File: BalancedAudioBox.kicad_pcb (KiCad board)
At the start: 2 copper layers, 26 parts, among them IC1 TPS61240IDRVRQ1, IC2 DRV135UA_2K5, J1 Conn_02x10_Odd_Even, U1 LM27762, U2 PCM5102

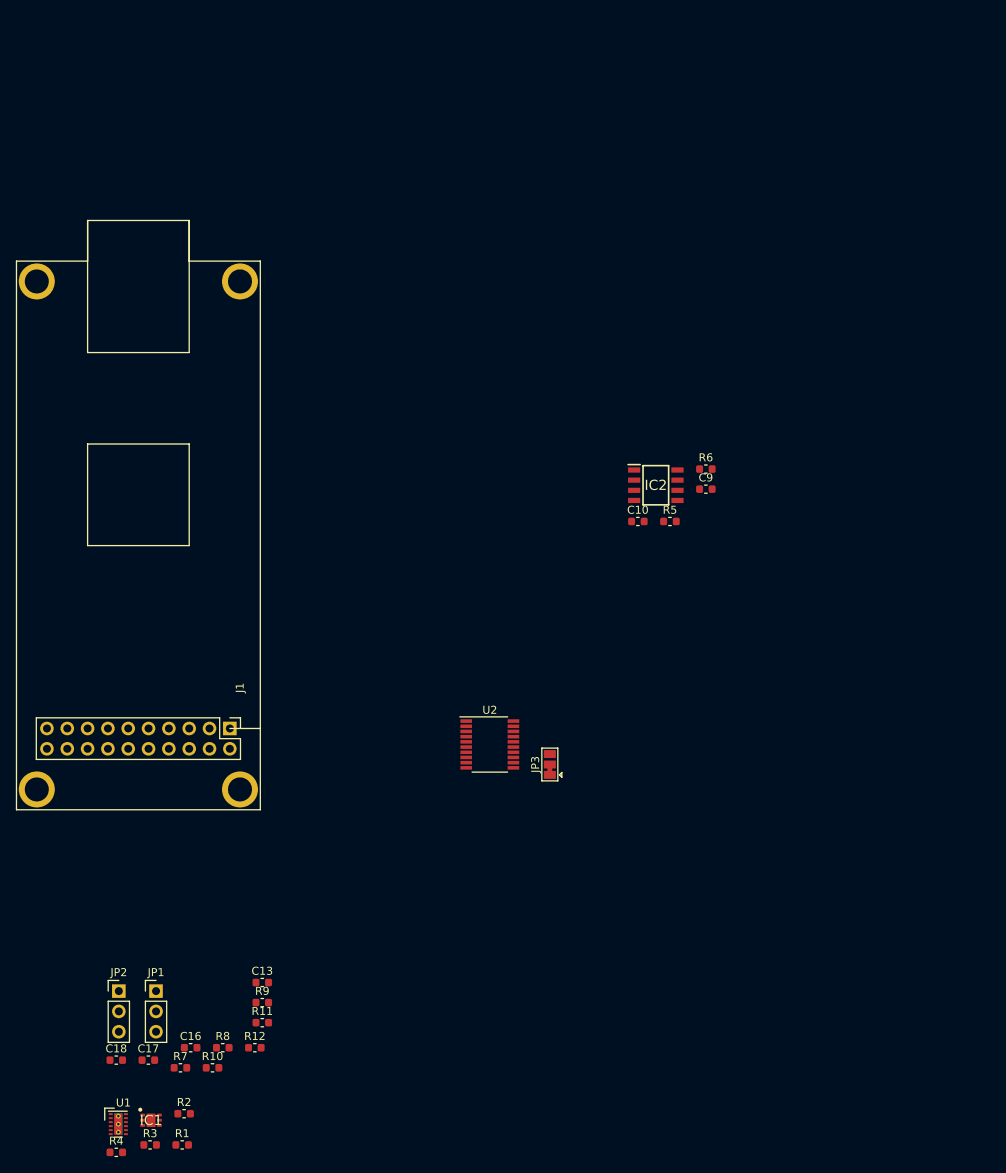
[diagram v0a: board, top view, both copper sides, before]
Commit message: adding PCB libraries
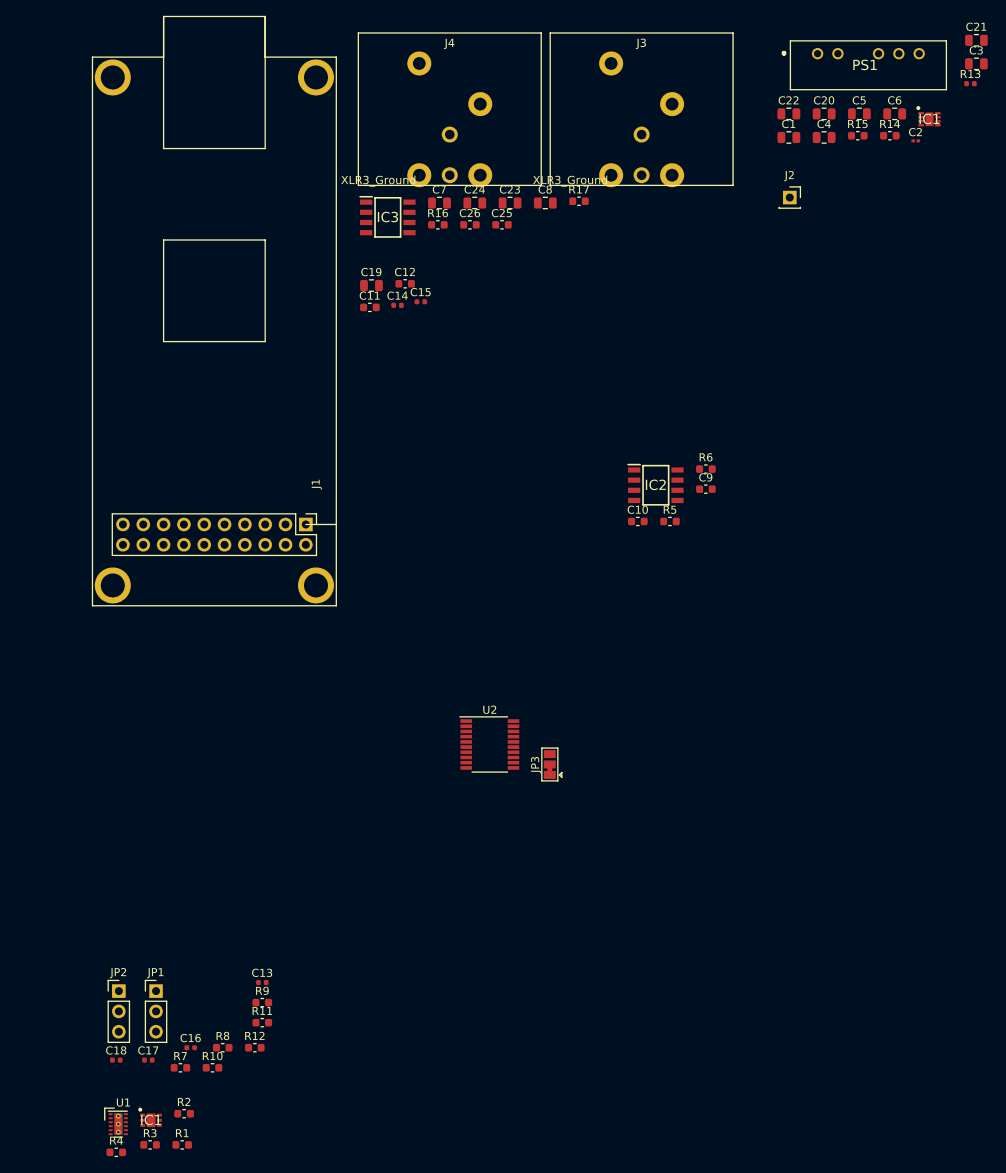
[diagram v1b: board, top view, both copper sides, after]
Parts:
- added C1: 10u/25V, Capacitor_SMD:C_0805_2012Metric, F.Cu at (191.9, 33.6)
- added C11: 2.2u, Capacitor_SMD:C_0603_1608Metric, F.Cu at (139.5, 54.9)
- added C12: 2.2u, Capacitor_SMD:C_0603_1608Metric, F.Cu at (143.9, 51.9)
- added C14: 2.2n, Capacitor_SMD:C_0402_1005Metric, F.Cu at (143.0, 54.6)
- added C15: 2.2n, Capacitor_SMD:C_0402_1005Metric, F.Cu at (145.9, 54.2)
- added C19: 10u/25V, Resistor_SMD:R_0805_2012Metric, F.Cu at (139.7, 52.1)
- added C2: 100p, Capacitor_SMD:C_0201_0603Metric, F.Cu at (207.7, 34.0)
- added C20: 10u/25V, Capacitor_SMD:C_0805_2012Metric, F.Cu at (196.3, 30.7)
- added C21: 4.7u, Capacitor_SMD:C_0805_2012Metric, F.Cu at (215.3, 21.5)
- added C22: 4.7u, Capacitor_SMD:C_0805_2012Metric, F.Cu at (191.9, 30.7)
- added C23: 4.7u, Capacitor_SMD:C_0805_2012Metric, F.Cu at (157.0, 41.8)
- added C24: 4.7u, Capacitor_SMD:C_0805_2012Metric, F.Cu at (152.6, 41.8)
- added C25: 100n, Capacitor_SMD:C_0603_1608Metric, F.Cu at (156.0, 44.5)
- added C26: 100n, Capacitor_SMD:C_0603_1608Metric, F.Cu at (152.0, 44.5)
- added C3: 4.7u, Capacitor_SMD:C_0805_2012Metric, F.Cu at (215.3, 24.4)
- added C4: 10u/25V, Capacitor_SMD:C_0805_2012Metric, F.Cu at (196.3, 33.6)
- added C5: 10u/25V, Capacitor_SMD:C_0805_2012Metric, F.Cu at (200.7, 30.7)
- added C6: 10u/25V, Capacitor_SMD:C_0805_2012Metric, F.Cu at (205.1, 30.7)
- added C7: 4.7u, Capacitor_SMD:C_0805_2012Metric, F.Cu at (148.2, 41.8)
- added C8: 4.7u, Capacitor_SMD:C_0805_2012Metric, F.Cu at (161.4, 41.8)
- added IC1: TPS61252DSGT, SamacSys_PCB_Library:SON50P200X200X80-9N, F.Cu at (209.5, 31.4)
- added IC3: DRV135UA_2K5, SamacSys_PCB_Library:SOIC127P600X175-8N, F.Cu at (141.8, 43.6)
- added J2: Conn_01x02, Connector_PinSocket_2.54mm:PinSocket_1x01_P2.54mm_Vertical, F.Cu at (192.0, 41.1)
- added J3: XLR3_Ground, BalancedAudioBox:XLR-NC3MA, F.Cu at (173.5, 30.1)
- added J4: XLR3_Ground, BalancedAudioBox:XLR-NC3MA, F.Cu at (149.5, 30.1)
- added PS1: DPU01L-15, SamacSys_PCB_Library:DPU01L15, F.Cu at (195.5, 23.2)
- added R13: 47k, Resistor_SMD:R_0402_1005Metric, F.Cu at (214.6, 26.9)
- added R14: 634k, Resistor_SMD:R_0603_1608Metric, F.Cu at (204.5, 33.4)
- added R15: 180k, Resistor_SMD:R_0603_1608Metric, F.Cu at (200.5, 33.4)
- added R16: 300R, Resistor_SMD:R_0603_1608Metric, F.Cu at (148.0, 44.5)
- added R17: 300R, Resistor_SMD:R_0603_1608Metric, F.Cu at (165.6, 41.6)
- C13, C16, C17, C18: footprint Capacitor_SMD:C_0603_1608Metric -> Capacitor_SMD:C_0402_1005Metric
- R1, R2: value R -> 1.58M
- R3, R4: value R -> 499k
- moved J1 27.2 mm to (131.5, 82.0)
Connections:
- C10 pad 1: Net-(C10-Pad1) -> -5V
- C9 pad 1: Net-(C9-Pad1) -> +5V

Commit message: placement complete
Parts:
- removed the IC1 at (112.2, 156.5)
- removed the IC1 at (209.5, 31.4)
- added C27: 10u/25V, Capacitor_SMD:C_0805_2012Metric, F.Cu at (143.0, 96.0)
- added IC1: TPS61252DSGT, BalancedAudioBox:SON50P200X200X80-9N, F.Cu at (148.0, 96.0)
- added J5: Conn_01x03, Connector_PinHeader_2.54mm:PinHeader_1x03_P2.54mm_Vertical, F.Cu at (174.5, 95.0)
- added J6: Conn_01x02, Connector_PinSocket_2.54mm:PinSocket_1x02_P2.54mm_Vertical, F.Cu at (148.0, 107.5)
- added L1: 1.5u, BalancedAudioBox:SRN30151R5Y, F.Cu at (146.6, 91.5)
- C10, C25, C26, C9: footprint Capacitor_SMD:C_0603_1608Metric -> Capacitor_SMD:C_0402_1005Metric
- C11, C12: footprint Capacitor_SMD:C_0603_1608Metric -> Capacitor_SMD:C_0805_2012Metric
- C19: footprint Resistor_SMD:R_0805_2012Metric -> Capacitor_SMD:C_0805_2012Metric
- C2: footprint Capacitor_SMD:C_0201_0603Metric -> Capacitor_SMD:C_0603_1608Metric
- IC2, IC3: footprint SamacSys_PCB_Library:SOIC127P600X175-8N -> Package_SO:SOIC-8_3.9x4.9mm_P1.27mm
- J2: value Conn_01x02 -> Conn_01x03; footprint Connector_PinSocket_2.54mm:PinSocket_1x01_P2.54mm_Vertical -> Connector_PinHeader_2.54mm:PinHeader_1x03_P2.54mm_Vertical
- PS1: footprint SamacSys_PCB_Library:DPU01L15 -> BalancedAudioBox:DPU01L15
- R10, R11, R12, R7, R8, R9: footprint Resistor_SMD:R_0603_1608Metric -> Resistor_SMD:R_0402_1005Metric
- moved PS1 119.1 mm to (145.0, 131.0)
- moved C21 115.0 mm to (145.0, 112.5), turned to 180 degrees
- moved C3 113.1 mm to (147.0, 114.5)
- moved C20 102.7 mm to (147.5, 121.0), turned to 270 degrees
- moved C6 98.7 mm to (147.0, 110.5), turned to 180 degrees
- moved C22 98.7 mm to (150.0, 120.0), turned to 90 degrees
- moved R13 93.3 mm to (152.5, 96.5), turned to 270 degrees
- moved C5 91.2 mm to (146.5, 104.0), turned to 180 degrees
- moved C19 86.6 mm to (181.5, 128.0)
- moved C2 86.4 mm to (152.5, 100.5), turned to 90 degrees
- moved R14 86.1 mm to (150.5, 100.5), turned to 90 degrees
- moved C4 84.2 mm to (146.5, 101.5), turned to 180 degrees
- moved R15 80.9 mm to (150.5, 97.0), turned to 90 degrees
- moved C1 78.0 mm to (145.0, 96.0), turned to 270 degrees
- moved C18 77.0 mm to (181.0, 125.0)
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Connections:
- net Net-(C2-Pad1) renamed /PowerSupply/VOUT-5.4V
- net Net-(C2-Pad2) renamed /PowerSupply/FB
- net Net-(C20-Pad1) renamed /PowerSupply/CP
- net Net-(R1-Pad2) renamed /PowerSupply/FB+
- net Net-(R2-Pad2) renamed /PowerSupply/FB-
- J2 pad 1: /PowerSupply/VIN -> +3V3
- PS1 pad 1: Net-(PS1-Pad1) -> /PowerSupply/VIN
- PS1 pad 2: Net-(PS1-Pad2) -> GND
- PS1 pad 4: Net-(PS1-Pad4) -> -5V
- PS1 pad 5: Net-(PS1-Pad5) -> GND
- PS1 pad 6: Net-(PS1-Pad6) -> +5V
- R13 pad 2: Net-(IC1-Pad4) -> /PowerSupply/ILIM
- R7 pad 1: Net-(R7-Pad1) -> +3V3
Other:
- board outline added: 90 x 80 mm

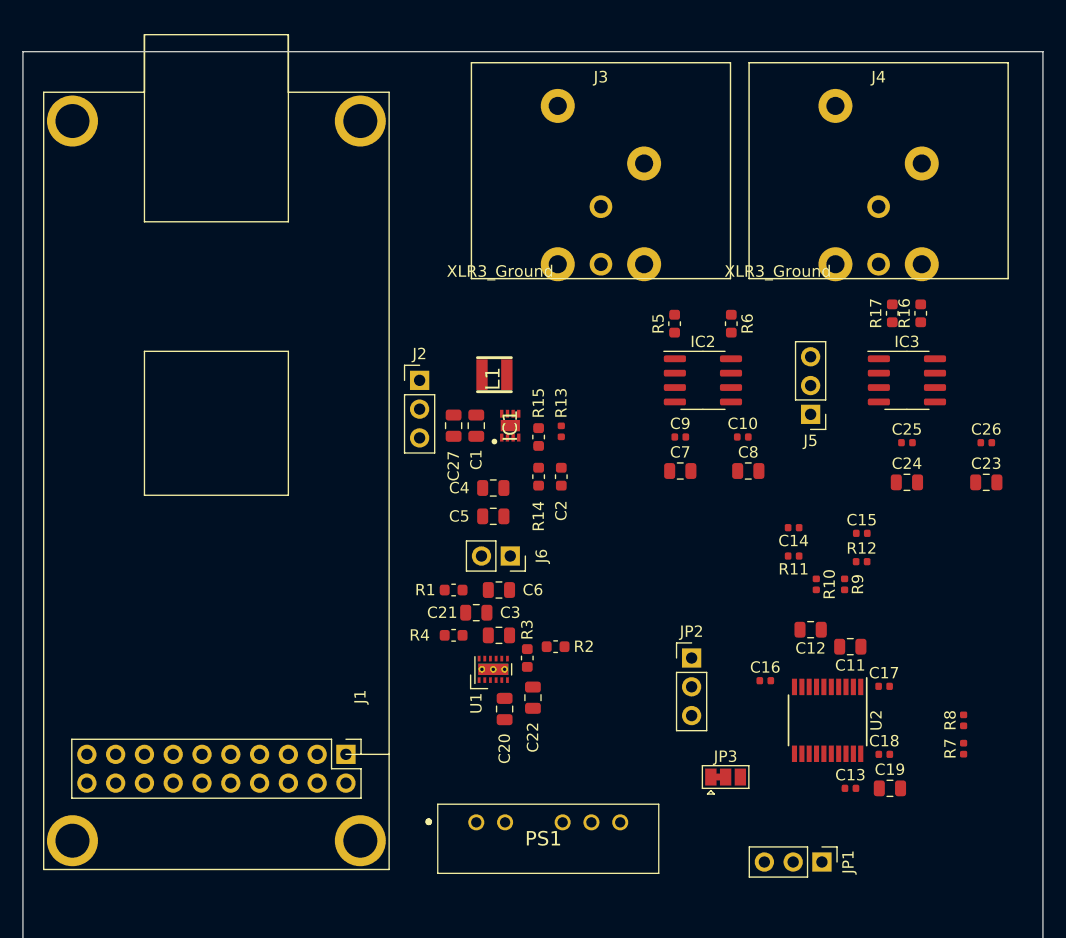
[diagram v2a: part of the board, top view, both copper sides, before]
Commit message: footprint and 3d improvements
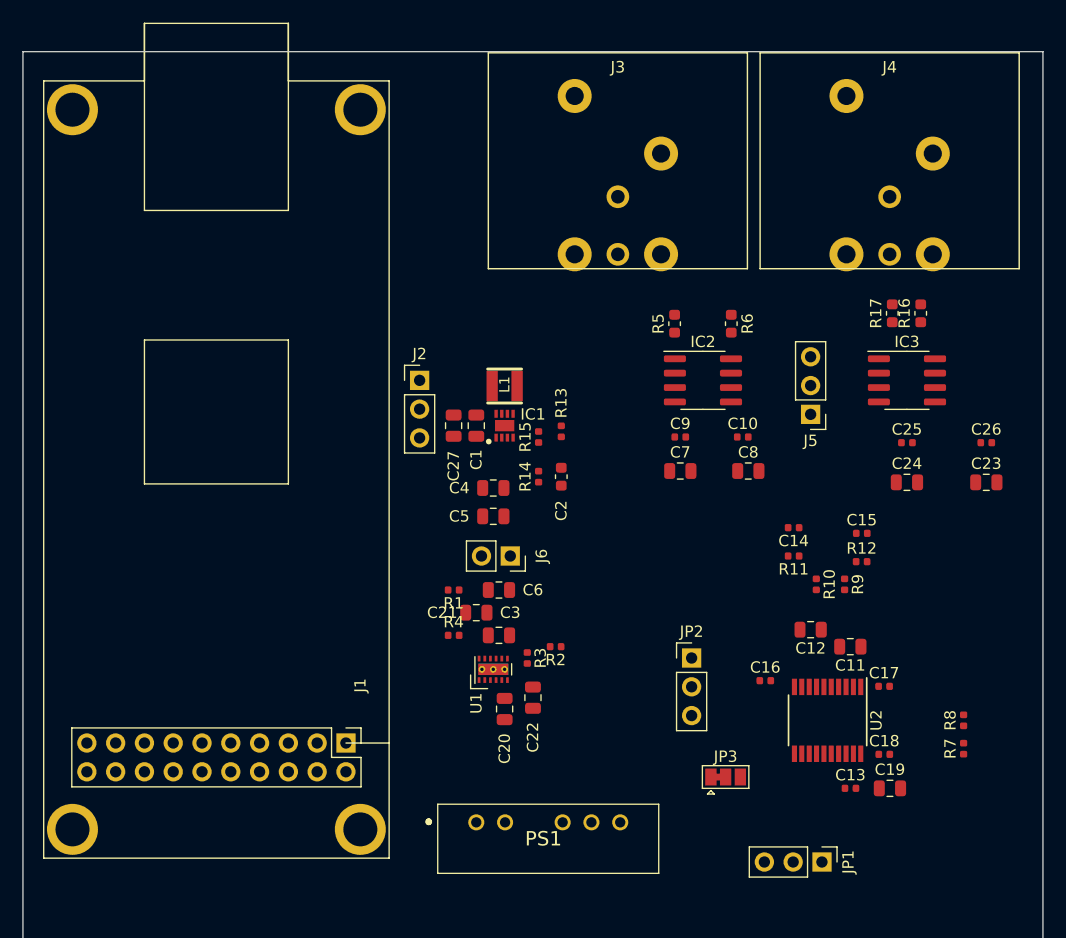
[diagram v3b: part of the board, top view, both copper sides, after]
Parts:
- R1, R14, R15, R2, R3, R4: footprint Resistor_SMD:R_0603_1608Metric -> Resistor_SMD:R_0402_1005Metric
- moved J3 1.73 mm to (157.5, 72.6)
- moved L1 1.35 mm to (147.5, 92.5), turned to 270 degrees
- moved J4 1.31 mm to (181.5, 72.6)
- moved J1 1.00 mm to (133.5, 124.0)
- moved IC1 0.50 mm to (147.5, 96.0)

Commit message: layout and silk
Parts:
- added J7: Conn_01x05, Connector_PinHeader_2.54mm:PinHeader_1x05_P2.54mm_Vertical, F.Cu at (146.5, 119.5)
- added J8: Conn_01x03, Connector_PinHeader_2.54mm:PinHeader_1x03_P2.54mm_Vertical, F.Cu at (169.0, 97.5)
- added REF**: MountingHole_3.2mm_M3, MountingHole:MountingHole_3.2mm_M3, F.Cu at (191.0, 131.0)
- added REF**: MountingHole_3.2mm_M3, MountingHole:MountingHole_3.2mm_M3, F.Cu at (109.0, 131.0)
- added REF**: MountingHole_3.2mm_M3, MountingHole:MountingHole_3.2mm_M3, F.Cu at (109.0, 67.0)
- added REF**: MountingHole_3.2mm_M3, MountingHole:MountingHole_3.2mm_M3, F.Cu at (191.0, 67.0)
- J6: footprint Connector_PinSocket_2.54mm:PinSocket_1x02_P2.54mm_Vertical -> Connector_PinHeader_2.54mm:PinHeader_1x02_P2.54mm_Vertical
- moved JP1 39.6 mm to (160.2, 98.0), turned to 0 degrees
- moved C20 35.3 mm to (182.8, 120.2), turned to 0 degrees
- moved R4 34.8 mm to (176.2, 124.8), turned to 90 degrees
- moved C27 33.0 mm to (159.2, 124.8), turned to 0 degrees
- moved U1 33.0 mm to (179.2, 121.2), turned to 180 degrees
- moved J2 32.6 mm to (151.5, 122.5)
- moved R1 32.5 mm to (172.2, 124.8), turned to 270 degrees
- moved C22 31.8 mm to (181.8, 117.8), turned to 180 degrees
- moved C21 31.0 mm to (174.2, 122.8), turned to 270 degrees
- moved L1 30.6 mm to (155.5, 122.0), turned to 180 degrees
- moved C1 30.3 mm to (159.2, 122.8), turned to 0 degrees
- moved C3 29.9 mm to (176.2, 120.8), turned to 90 degrees
- moved PS1 29.1 mm to (147.5, 102.0), turned to 90 degrees
- moved R3 28.8 mm to (178.2, 118.2), turned to 0 degrees
- moved C6 27.3 mm to (172.2, 120.8), turned to 270 degrees
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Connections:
- net /DAC/BCLK renamed /BCLK
- net /DAC/DIN renamed /DIN
- net /DAC/LRCLK renamed /LRCLK
- net Net-(IC2-Pad1) renamed /OutputDriver/LEFT_VON
- net Net-(IC2-Pad7) renamed /OutputDriver/LEFT_VOP
- net Net-(IC3-Pad1) renamed /OutputDriver/RIGHT_VON
- net Net-(IC3-Pad7) renamed /OutputDriver/RIGHT_VOP
- net Net-(J1-Pad10) renamed /MCLK
- net Net-(JP1-Pad2) renamed /DAC/LATENCY
- net Net-(JP2-Pad2) renamed /DAC/DEEMP
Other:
- board size 90 x 80 mm -> 90 x 72 mm
- rule trace_min: 0.2 -> 0.15
- board text added: "De-emp ON"
- board text added: "G"
- board text added: "GND"
- board text added: "L"
- board text added: "Latency Low"
- board text added: "Normal"
- board text added: "Off"
- board text added: "R"
- board text added: "Vin"

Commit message: adding regulator
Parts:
- R7: value 7k5 -> 2k2
- R8: value 2k7 -> 3k3
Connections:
- C1 pad 1: /PowerSupply/VIN -> VIN
- C27 pad 1: /PowerSupply/VIN -> VIN
- IC1 pad 6: /PowerSupply/VIN -> VIN
- IC1 pad 8: /PowerSupply/VIN -> VIN
- J2 pad 2: /PowerSupply/VIN -> VIN
- L1 pad 1: /PowerSupply/VIN -> VIN
- PS1 pad 1: /PowerSupply/VIN -> VIN
- R7 pad 1: +3V3 -> VIN

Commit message: more layout
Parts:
- removed the REF** at (109.0, 131.0)
- removed the REF** at (109.0, 67.0)
- removed the REF** at (191.0, 67.0)
- added JP4: SolderJumper_3_Bridged12, Jumper:SolderJumper-3_P1.3mm_Bridged12_Pad1.0x1.5mm, F.Cu at (166.2, 112.5)
- added U3: AP1117-33, Package_TO_SOT_SMD:SOT-223-3_TabPin2, F.Cu at (167.5, 106.5)
- J2: value Conn_01x03 -> Conn_01x02; footprint Connector_PinHeader_2.54mm:PinHeader_1x03_P2.54mm_Vertical -> Connector_PinHeader_2.54mm:PinHeader_1x02_P2.54mm_Vertical
- moved JP2 28.9 mm to (184.5, 102.5)
- moved JP1 28.6 mm to (188.5, 102.5)
- moved C22 28.4 mm to (158.5, 101.5)
- moved C20 27.7 mm to (160.8, 103.5)
- moved R3 27.4 mm to (156.2, 102.0), turned to 270 degrees
- moved C3 27.3 mm to (154.8, 104.0)
- moved U1 27.2 mm to (157.5, 105.0)
- moved J5 26.9 mm to (161.2, 90.5)
- moved R2 26.6 mm to (155.0, 101.2)
- moved J4 25.3 mm to (156.0, 72.5)
- moved R1 25.1 mm to (152.8, 109.0)
- moved R4 25.1 mm to (156.8, 109.0)
- moved C21 24.8 mm to (154.8, 107.5), turned to 90 degrees
- moved J3 23.6 mm to (179.0, 72.5)
- moved J7 22.5 mm to (167.5, 127.5)
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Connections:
- net /PowerSupply/VOUT-5.4V renamed VOUT-5.4V
- C17 pad 1: +3V3 -> +3.3VA
- C18 pad 1: +3V3 -> +3.3VA
- C19 pad 1: +3V3 -> +3.3VA
- J2 pad 1: +3V3 -> GND
- U2 pad 1: +3V3 -> +3.3VA
- U2 pad 8: +3V3 -> +3.3VA
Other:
- board size 90 x 72 mm -> 81 x 73 mm
- board text added: "min 4.0V"
- board text removed: "G"
- board text removed: "Normal"
- board text removed: "Off"

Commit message: some routing
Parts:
- J7: value Conn_01x05 -> Conn_01x06; footprint Connector_PinHeader_2.54mm:PinHeader_1x05_P2.54mm_Vertical -> Connector_PinHeader_2.54mm:PinHeader_1x06_P2.54mm_Vertical
- moved R1 17.6 mm to (157.2, 92.0)
- moved J2 15.8 mm to (150.8, 115.0), turned to 0 degrees
- moved J7 7.60 mm to (166.2, 120.0), turned to 90 degrees
- moved R2 3.58 mm to (158.2, 99.8), turned to 180 degrees
- moved R5 2.69 mm to (179.0, 85.0), turned to 90 degrees
- moved JP4 2.24 mm to (164.2, 113.5)
- moved R4 1.58 mm to (157.2, 107.5), turned to 180 degrees
- moved R13 1.50 mm to (155.5, 118.0)
- moved R15 1.50 mm to (154.0, 118.0)
- moved R7 1.25 mm to (176.5, 112.2)
- moved R8 1.06 mm to (175.2, 112.2)
- moved R6 1.00 mm to (181.5, 85.0)
- moved C6 0.90 mm to (161.0, 105.8), turned to 0 degrees
- moved C21 0.56 mm to (154.2, 107.2), turned to 0 degrees
- moved C22 0.50 mm to (159.0, 101.5)
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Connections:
- net VOUT-5.4V renamed +5.4V
- J7 pad 5: GND -> +3V3
- R7 pad 1: VIN -> Net-(JP4-Pad2)
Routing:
- net GND: track 0.00 -> 104.4 mm
- net +3V3: track 0.00 -> 70.4 mm, vias 0 -> 1
- net /DIN: track 0.00 -> 70.4 mm
- net +5V: track 0.00 -> 67.5 mm
- net /BCLK: track 0.00 -> 65.3 mm
- net /LRCLK: track 0.00 -> 63.4 mm, vias 0 -> 1
- net -5V: track 0.00 -> 59.3 mm, vias 0 -> 5
- net /MCLK: track 0.00 -> 52.2 mm
- net VIN: track 0.00 -> 26.7 mm
- net /PowerSupply/FB+: track 0.00 -> 26.4 mm
- net +3.3VA: track 0.00 -> 25.6 mm
- net Net-(JP4-Pad2): track 0.00 -> 24.7 mm, vias 0 -> 2
- net +5.4V: track 0.00 -> 22.6 mm
- net Net-(J4-Pad2): track 0.00 -> 18.5 mm
- net /DAC/LATENCY: track 0.00 -> 18.4 mm
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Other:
- net class Default: clearance 0.2 -> 0.15; trace_width 0.25 -> 0.5
- net class Power added: clearance 0.2, trace_width 0.6, via_dia 0.8, via_drill 0.4
- rule trace_clearance: 0.2 -> 0.15

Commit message: full route
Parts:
- added C28: 100n, Capacitor_SMD:C_0402_1005Metric, F.Cu at (168.8, 101.2)
- moved C27 17.7 mm to (147.8, 110.8), turned to 0 degrees
- moved L1 8.50 mm to (150.8, 118.5), turned to 180 degrees
- moved C21 7.81 mm to (155.2, 99.5), turned to 180 degrees
- moved C3 6.60 mm to (158.8, 99.0), turned to 0 degrees
- moved C1 6.33 mm to (155.2, 119.8), turned to 0 degrees
- moved R4 5.26 mm to (155.0, 102.8), turned to 90 degrees
- moved C2 5.06 mm to (158.8, 113.2), turned to 180 degrees
- moved R15 5.06 mm to (155.8, 113.2), turned to 180 degrees
- moved C5 4.37 mm to (160.2, 117.2), turned to 270 degrees
- moved C6 4.28 mm to (156.8, 105.2), turned to 270 degrees
- moved R3 3.58 mm to (160.2, 101.2)
- moved IC1 3.26 mm to (155.0, 117.0), turned to 180 degrees
- moved R13 3.26 mm to (155.8, 114.8), turned to 0 degrees
- moved R2 3.09 mm to (161.2, 99.0), turned to 270 degrees
- moved C22 3.04 mm to (162.0, 102.0), turned to 90 degrees
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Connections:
- net Net-(IC1-Pad7) renamed /PowerSupply/SW
- U1 pad 13: Net-(U1-Pad13) -> GND
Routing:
- net GND: track 104.4 -> 118.4 mm, vias 0 -> 39
- net +5.4V: track 22.6 -> 12.1 mm, vias 0 -> 3
- net /PowerSupply/FB+: track 26.4 -> 15.9 mm
- net +5V: track 67.5 -> 57.6 mm
- net +3.3VA: track 25.6 -> 30.1 mm
- net /PowerSupply/SW: track 0.00 -> 3.05 mm
- net /PowerSupply/FB-: track 5.35 -> 3.09 mm
- net VIN: track 26.7 -> 28.4 mm, vias 0 -> 2
- net -5V: track 59.3 -> 60.6 mm
- net Net-(C3-Pad2): track 2.21 -> 3.31 mm
- net /DAC/DEEMP: track 17.1 -> 16.0 mm, vias 2 -> 1
- added copper zone on F.Cu, net +5.4V
- added copper zone on B.Cu, net GND
- added copper zone on F.Cu, net GND
- added copper zone on F.Cu, net VIN
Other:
- board text added: "GND tie"
- board text removed: "R"
